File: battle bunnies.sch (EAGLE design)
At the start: 59 parts, among them IC1 CP2104, Q1 mmbt2222, Q2 mmbt2222, SW2 KMR2, U1 PCA9685, U2 SPX3819, U3 MCP73831T-2ACI/OT, X2 ESP-12, X4 20329

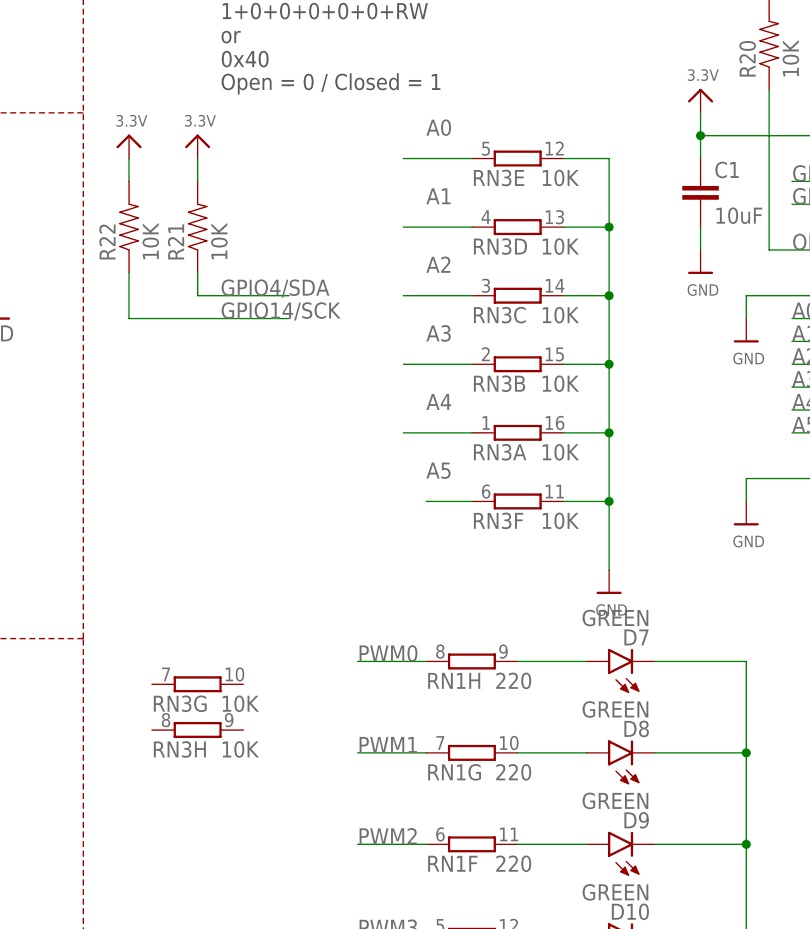
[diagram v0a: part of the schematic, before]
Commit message: Adding values to the RNs that were missing
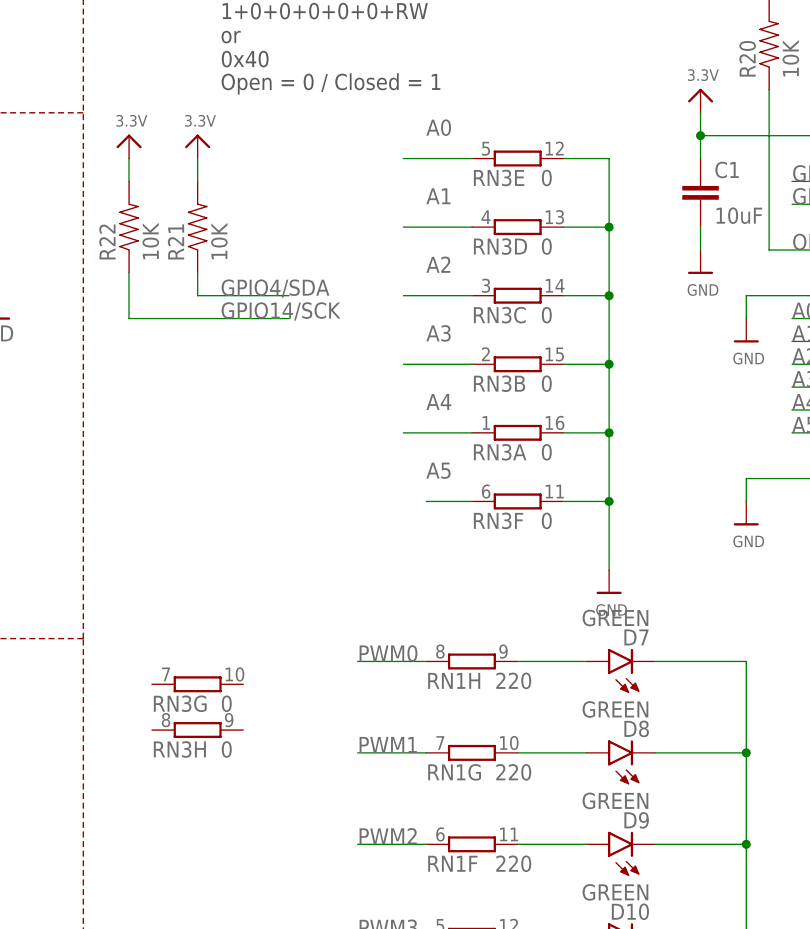
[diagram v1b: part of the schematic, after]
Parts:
- RN3: value 10K -> 0
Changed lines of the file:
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@@
 <part name="RN1" library="resistor-dil" deviceset="8R-N" device="EXB2HV" value="220"/>
 <part name="RN2" library="resistor-dil" deviceset="8R-N" device="EXB2HV" value="220"/>
-<part name="RN3" library="resistor-dil" deviceset="8R-N" device="EXB2HV" value="10K"/>
+<part name="RN3" library="resistor-dil" deviceset="8R-N" device="EXB2HV" value="0"/>
 </parts>
 <sheets>
